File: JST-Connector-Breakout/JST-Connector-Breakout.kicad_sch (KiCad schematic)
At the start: 28 parts, among them CN1 JST SHD 2x08, CN10 JST GH 1x06, CN2 JST GH 1x03, CN3 JST GH 1x08, CN5 JST GH 1x02, CN6 JST GH 1x03, CN7 JST XH 1x02, CN8 JST SHD 2x08, CN9 JST GH 1x03, J1 Conn_01x02_Pin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

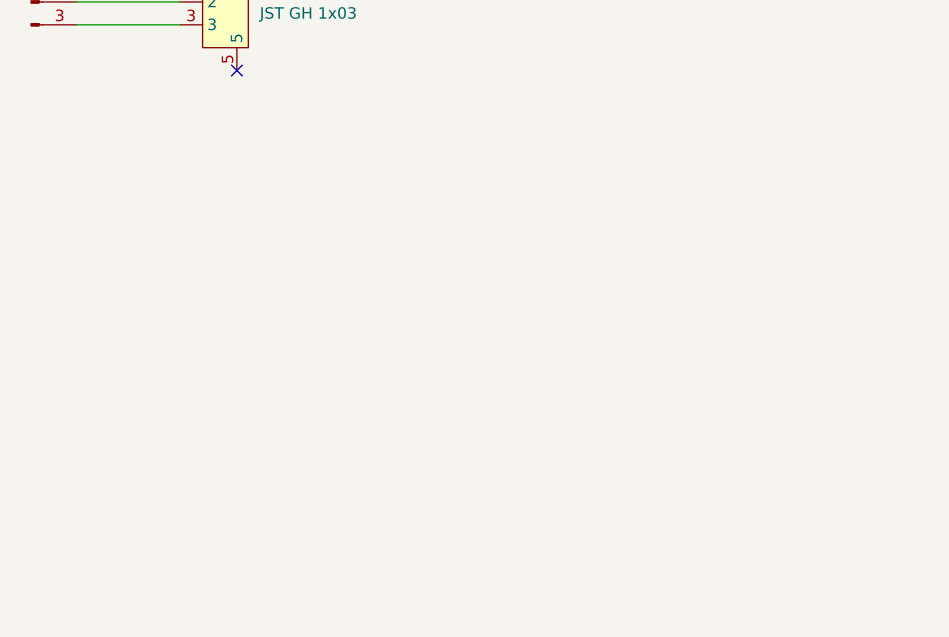
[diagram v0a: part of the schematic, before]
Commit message: PCB panelizing with mouse bites
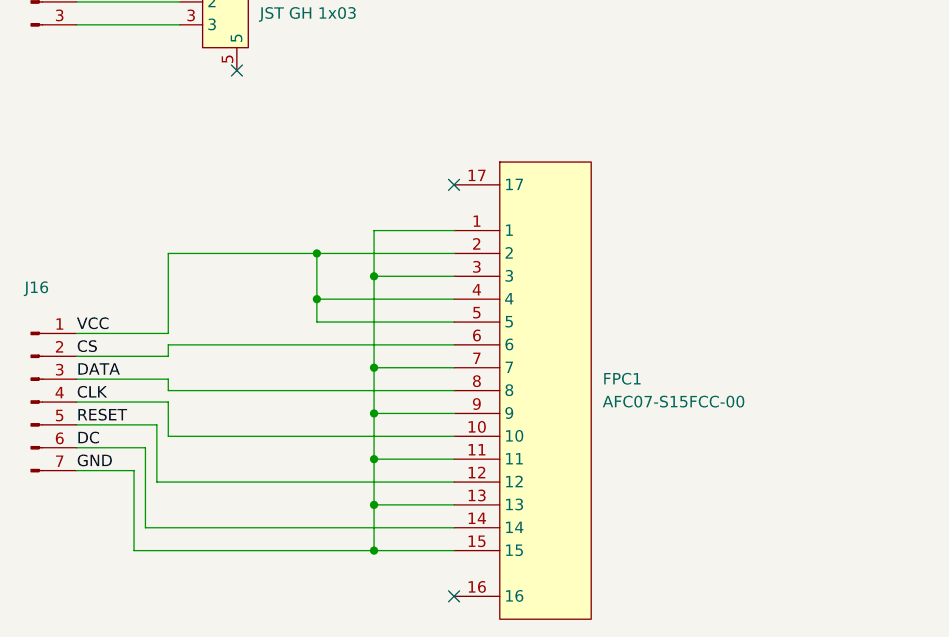
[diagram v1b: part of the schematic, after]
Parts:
- added FPC1: AFC07-S15FCC-00, easyeda2kicad:FPC-SMD_AFC07-S15FCC-00, symbol easyeda2kicad:AFC07-S15FCC-00
- added J16: Conn_01x07_Pin, Connector_PinHeader_2.54mm:PinHeader_1x07_P2.54mm_Vertical, symbol Connector:Conn_01x07_Pin
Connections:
- new net CLK: FPC1.10, J16.4 (Pin_4)
- new net CS: FPC1.6, J16.2 (Pin_2)
- new net DATA: FPC1.8, J16.3 (Pin_3)
- new net DC: FPC1.14, J16.6 (Pin_6)
- new net GND: FPC1.1, FPC1.11, FPC1.13, FPC1.15, FPC1.3, FPC1.7, FPC1.9, J16.7 (Pin_7)
- new net RESET: FPC1.12, J16.5 (Pin_5)
- new net VCC: FPC1.2, FPC1.4, FPC1.5, J16.1 (Pin_1)
- no-connect marks 28 -> 30

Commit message: Refine BOM and fabrication settings for JST breakout
- Exclude non-fitted/connector parts from BOM (in_bom no)
- Add Mfr. Part # for JST connector
- Auto-place schematic net labels
- Enable EXCLUDE DNP in fabrication toolkit
- Regenerate production gerbers and add design backups
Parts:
- CN10: Mfr. Part # (none) -> HC-1.25-6PWT
- J1, J10, J11, J12, J13, J14, J16, J2, J3, J4, J5, J6, J7, J8, J9: now left out of the parts list
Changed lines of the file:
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@@
 	(label "VCC"
 		(at 36.83 146.05 0)
+		(fields_autoplaced yes)
 		(effects
 			(font
@@
 	(label "CS"
 		(at 36.83 148.59 0)
+		(fields_autoplaced yes)
 		(effects
 			(font
@@
 	(label "DATA"
 		(at 36.83 151.13 0)
+		(fields_autoplaced yes)
 		(effects
 			(font
@@
 	(label "CLK"
 		(at 36.83 153.67 0)
+		(fields_autoplaced yes)
 		(effects
 			(font
@@
 	(label "DC"
 		(at 36.83 158.75 0)
+		(fields_autoplaced yes)
 		(effects
 			(font
@@
 	(label "GND"
 		(at 36.83 161.29 0)
+		(fields_autoplaced yes)
 		(effects
 			(font
@@
 	(label "RESET"
 		(at 36.83 156.21 0)
+		(fields_autoplaced yes)
 		(effects
 			(font
@@
 		(unit 1)
 		(exclude_from_sim no)
-		(in_bom yes)
+		(in_bom no)
 		(on_board yes)
 		(dnp no)
@@
 		(unit 1)
 		(exclude_from_sim no)
-		(in_bom yes)
+		(in_bom no)
 		(on_board yes)
 		(dnp no)
@@
 		(unit 1)
 		(exclude_from_sim no)
-		(in_bom yes)
+		(in_bom no)
 		(on_board yes)
 		(dnp no)
@@
 		(unit 1)
 		(exclude_from_sim no)
-		(in_bom yes)
+		(in_bom no)
 		(on_board yes)
 		(dnp no)
@@
 			)
 		)
+		(property "Mfr. Part #" "HC-1.25-6PWT"
+			(at 53.34 36.83 0)
+			(effects
+				(font
+					(size 1.27 1.27)
+				)
+				(hide yes)
+			)
+		)
 		(pin "3"
 		)
@@
 		(unit 1)
 		(exclude_from_sim no)
-		(in_bom yes)
+		(in_bom no)
 		(on_board yes)
 		(dnp no)
@@
 		(unit 1)
 		(exclude_from_sim no)
-		(in_bom yes)
+		(in_bom no)
 		(on_board yes)
 		(dnp no)
@@
 		(unit 1)
 		(exclude_from_sim no)
-		(in_bom yes)
+		(in_bom no)
 		(on_board yes)
 		(dnp no)
@@
 		(unit 1)
 		(exclude_from_sim no)
-		(in_bom yes)
+		(in_bom no)
 		(on_board yes)
 		(dnp no)
@@
 		(unit 1)
 		(exclude_from_sim no)
-		(in_bom yes)
+		(in_bom no)
 		(on_board yes)
 		(dnp no)
@@
 		(unit 1)
 		(exclude_from_sim no)
-		(in_bom yes)
+		(in_bom no)
 		(on_board yes)
 		(dnp no)
@@
 		(unit 1)
 		(exclude_from_sim no)
-		(in_bom yes)
+		(in_bom no)
 		(on_board yes)
 		(dnp no)
@@
 		(unit 1)
 		(exclude_from_sim no)
-		(in_bom yes)
+		(in_bom no)
 		(on_board yes)
 		(dnp no)
@@
 		(unit 1)
 		(exclude_from_sim no)
-		(in_bom yes)
+		(in_bom no)
 		(on_board yes)
 		(dnp no)
@@
 		(unit 1)
 		(exclude_from_sim no)
-		(in_bom yes)
+		(in_bom no)
 		(on_board yes)
 		(dnp no)
@@
 		(unit 1)
 		(exclude_from_sim no)
-		(in_bom yes)
-		(on_board yes)
-		(dnp no)
+		(in_bom no)
+		(on_board yes)
+		(dnp no)
